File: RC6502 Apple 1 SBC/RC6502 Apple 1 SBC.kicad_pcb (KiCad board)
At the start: 2 copper layers, 99.1 x 99.7 mm, 43 parts, among them J1 VP GND, J2 Arduino Nano, J3 Backplane, J4 Hole, J5 Hole, J6 Hole, J7 Hole, J8 Power, SW1 RESET, U1 WD65C02, U2 HM62256BLP-7, U3 74HCT138, U4 28C256, U5 74HCT00, U6 NE555, U7 74HCT04, U8 WD65C21, U9 MCP23S17, X1 1MHz

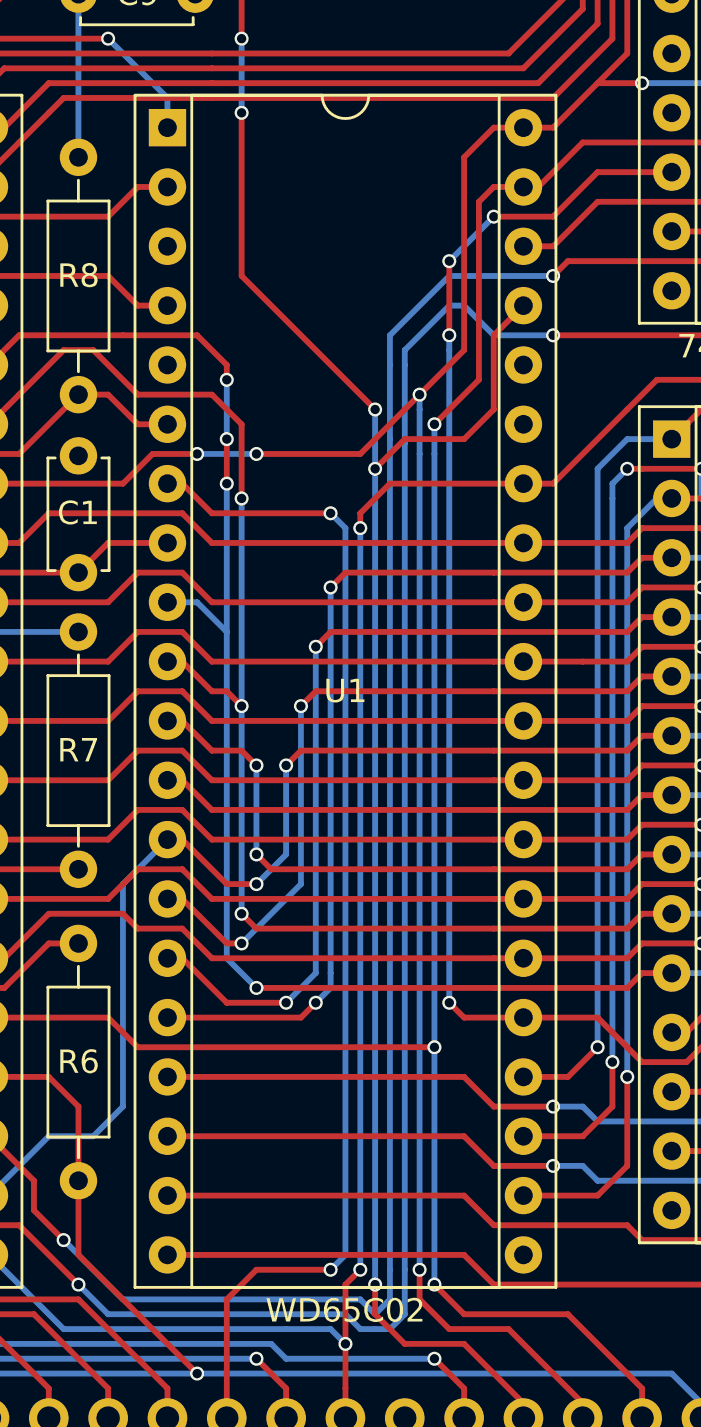
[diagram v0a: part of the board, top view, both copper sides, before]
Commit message: Added VP GND details to silkscreen.
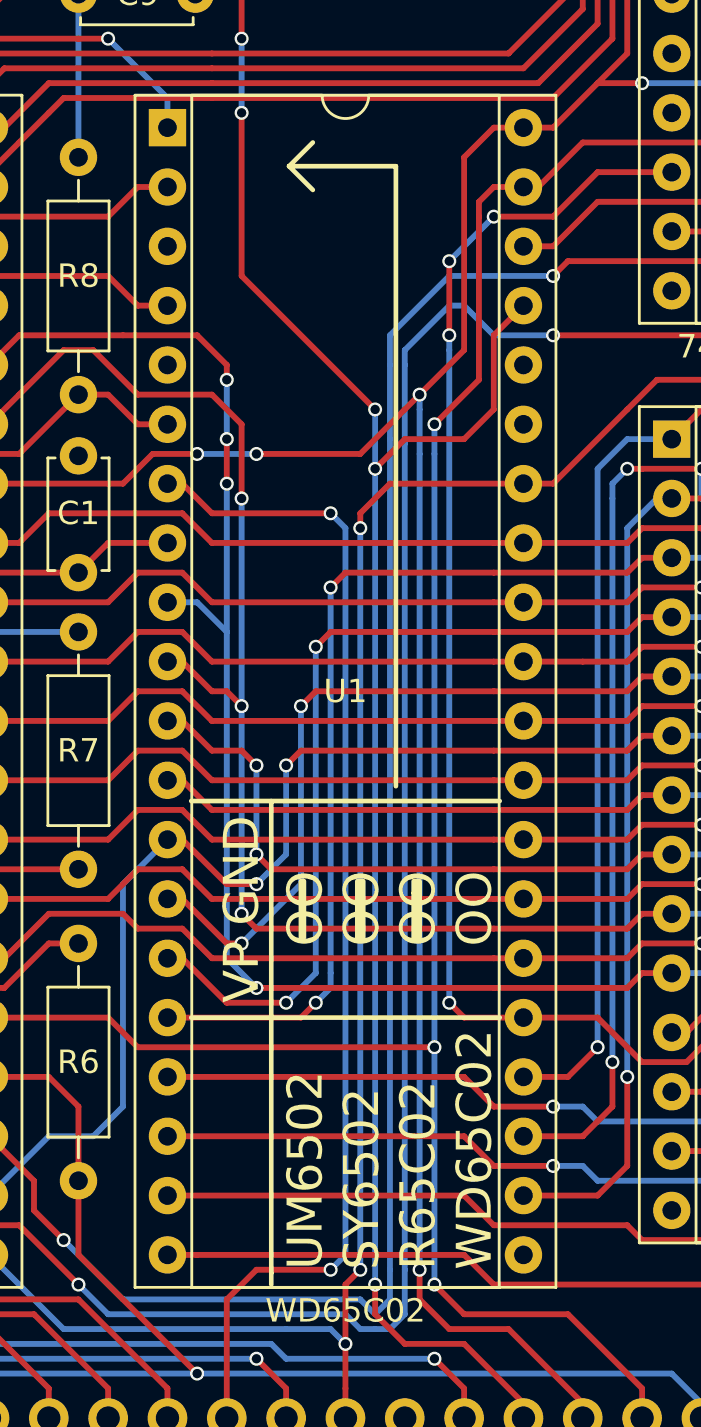
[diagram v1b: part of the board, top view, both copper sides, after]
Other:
- board text added: "OO OO OO OO"
- board text added: "UM6502 SY6502 R65C02 WD65C02"
- board text added: "VP GND"
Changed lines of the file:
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@@
     (links 229)
     (no_connects 0)
-    (area 114.23 35.22 220.820001 148.420001)
+    (area 116.129999 39.294999 215.340001 139.140001)
     (thickness 1.6)
-    (drawings 126)
+    (drawings 146)
     (tracks 1995)
     (zones 0)
@@
   (page A4)
   (layers
-    (0 F.Cu signal)
-    (31 B.Cu signal)
+    (0 F.Cu signal hide)
+    (31 B.Cu signal hide)
     (32 B.Adhes user)
     (33 F.Adhes user)
     (34 B.Paste user)
     (35 F.Paste user)
-    (36 B.SilkS user)
+    (36 B.SilkS user hide)
     (37 F.SilkS user)
     (38 B.Mask user)
@@
     )
   )
+  (gr_line (start 153.162 84.201) (end 154.178 85.217) (angle 90) (layer F.SilkS) (width 0.2))
+  (gr_line (start 153.162 84.201) (end 154.178 83.185) (angle 90) (layer F.SilkS) (width 0.2))
+  (gr_line (start 157.734 84.201) (end 153.162 84.201) (angle 90) (layer F.SilkS) (width 0.2))
+  (gr_line (start 157.734 110.744) (end 157.734 84.201) (angle 90) (layer F.SilkS) (width 0.2))
+  (gr_line (start 152.4 131.572) (end 152.4 132.08) (angle 90) (layer F.SilkS) (width 0.2))
+  (gr_line (start 156.337 117.221) (end 156.337 114.808) (angle 90) (layer F.SilkS) (width 0.2))
+  (gr_line (start 158.75 117.221) (end 158.75 114.808) (angle 90) (layer F.SilkS) (width 0.2))
+  (gr_line (start 158.496 115.316) (end 158.623 115.316) (angle 90) (layer F.SilkS) (width 0.2))
+  (gr_line (start 158.496 117.221) (end 158.496 114.808) (angle 90) (layer F.SilkS) (width 0.2))
+  (gr_line (start 158.623 117.221) (end 158.623 114.808) (angle 90) (layer F.SilkS) (width 0.2))
+  (gr_line (start 156.083 114.808) (end 156.083 117.221) (angle 90) (layer F.SilkS) (width 0.2))
+  (gr_line (start 156.21 117.221) (end 156.21 114.808) (angle 90) (layer F.SilkS) (width 0.2))
+  (gr_line (start 153.67 114.808) (end 153.67 117.221) (angle 90) (layer F.SilkS) (width 0.2))
+  (gr_line (start 153.797 114.808) (end 153.797 117.221) (angle 90) (layer F.SilkS) (width 0.2))
+  (gr_line (start 148.971 111.379) (end 162.179 111.379) (angle 90) (layer F.SilkS) (width 0.2))
+  (gr_line (start 148.971 120.65) (end 162.179 120.65) (angle 90) (layer F.SilkS) (width 0.2))
+  (gr_line (start 152.4 111.379) (end 152.4 131.572) (angle 90) (layer F.SilkS) (width 0.2))
+  (gr_text "VP GND" (at 151.13 120.015 90) (layer F.SilkS)
+    (effects (font (size 1.5 1.5) (thickness 0.2)) (justify left))
+  )
+  (gr_text "OO\nOO\nOO\nOO" (at 157.48 117.602 90) (layer F.SilkS)
+    (effects (font (size 1.5 1.5) (thickness 0.2)) (justify left))
+  )
+  (gr_text "UM6502\nSY6502\nR65C02\nWD65C02" (at 157.48 131.445 90) (layer F.SilkS)
+    (effects (font (size 1.5 1.5) (thickness 0.2)) (justify left))
+  )
   (gr_text "Backplane Connector" (at 156.21 134.62) (layer B.SilkS)

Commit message: Exported files with updated silkscreen
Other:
- board text added: "Jumper me when NOT using backplane"
- board text removed: "Jumper me when not using backplane"
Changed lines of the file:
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@@
     (area 116.129999 39.294999 215.340001 139.140001)
     (thickness 1.6)
-    (drawings 146)
+    (drawings 148)
     (tracks 1995)
     (zones 0)
@@
     (34 B.Paste user)
     (35 F.Paste user)
-    (36 B.SilkS user hide)
+    (36 B.SilkS user)
     (37 F.SilkS user)
     (38 B.Mask user)
@@
     )
   )
+  (gr_line (start 157.48 41.91) (end 158.75 41.91) (angle 90) (layer B.SilkS) (width 0.2))
+  (gr_line (start 157.48 46.99) (end 157.48 41.91) (angle 90) (layer B.SilkS) (width 0.2))
+  (gr_line (start 158.75 46.99) (end 157.48 46.99) (angle 90) (layer B.SilkS) (width 0.2))
+  (gr_text "Jumper me when\nNOT using backplane" (at 182.245 44.45) (layer B.SilkS)
+    (effects (font (size 1.5 1.5) (thickness 0.3)) (justify left mirror))
+  )
   (gr_line (start 153.162 84.201) (end 154.178 85.217) (angle 90) (layer F.SilkS) (width 0.2))
   (gr_line (start 153.162 84.201) (end 154.178 83.185) (angle 90) (layer F.SilkS) (width 0.2))
@@
   (gr_line (start 215.265 126.365) (end 212.725 126.365) (angle 90) (layer B.SilkS) (width 0.2))
   (gr_line (start 182.88 42.545) (end 182.88 46.355) (angle 90) (layer B.SilkS) (width 0.2))
-  (gr_text "Jumper me when\nnot using backplane" (at 182.245 44.45) (layer B.SilkS)
-    (effects (font (size 1.5 1.5) (thickness 0.3)) (justify left mirror))
-  )
   (gr_line (start 158.75 46.99) (end 186.055 46.99) (angle 90) (layer B.SilkS) (width 0.2))
-  (gr_line (start 158.75 41.91) (end 158.75 46.99) (angle 90) (layer B.SilkS) (width 0.2))
   (gr_line (start 186.055 41.91) (end 158.75 41.91) (angle 90) (layer B.SilkS) (width 0.2))
   (gr_line (start 186.055 46.99) (end 186.055 41.91) (angle 90) (layer B.SilkS) (width 0.2))

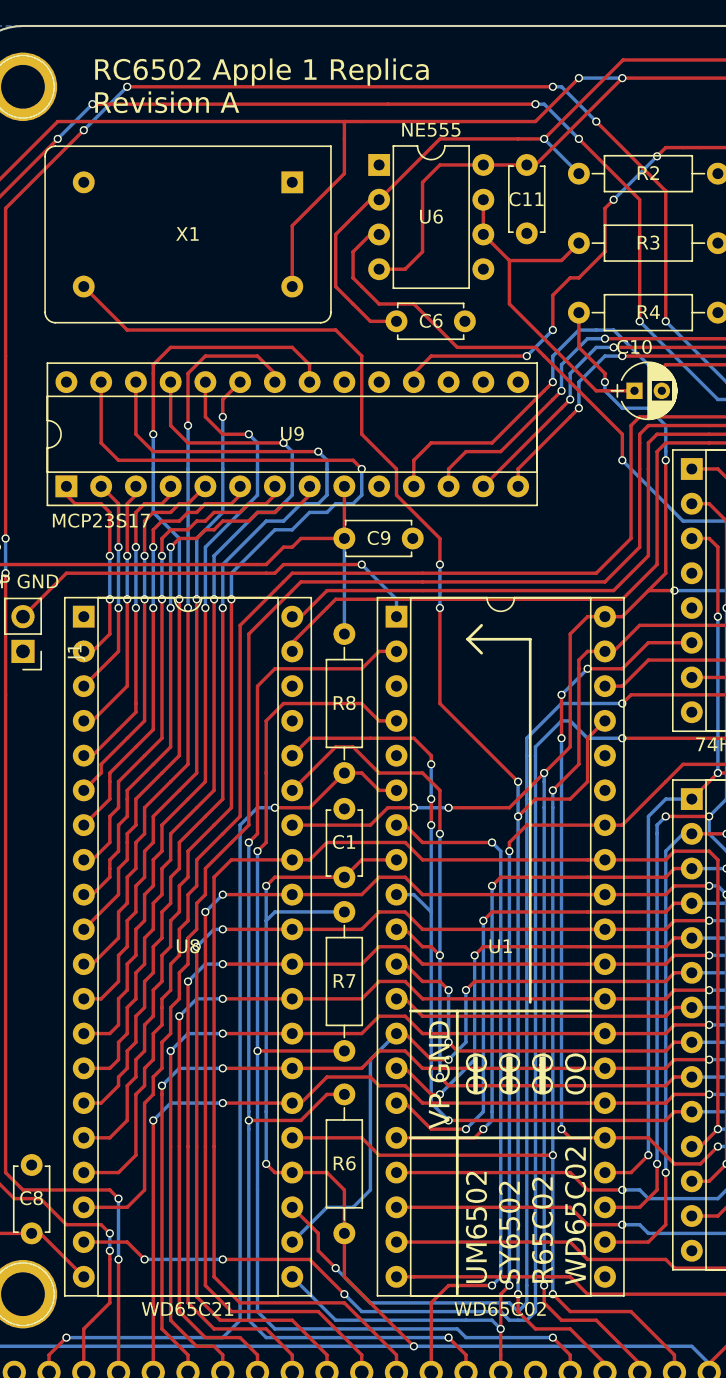
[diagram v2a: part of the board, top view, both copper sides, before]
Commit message: SBC Revision B
Revision A still don't work with W65c02 processors, added BE signal pull-up (untested wether this improves 65c02 compatibility).
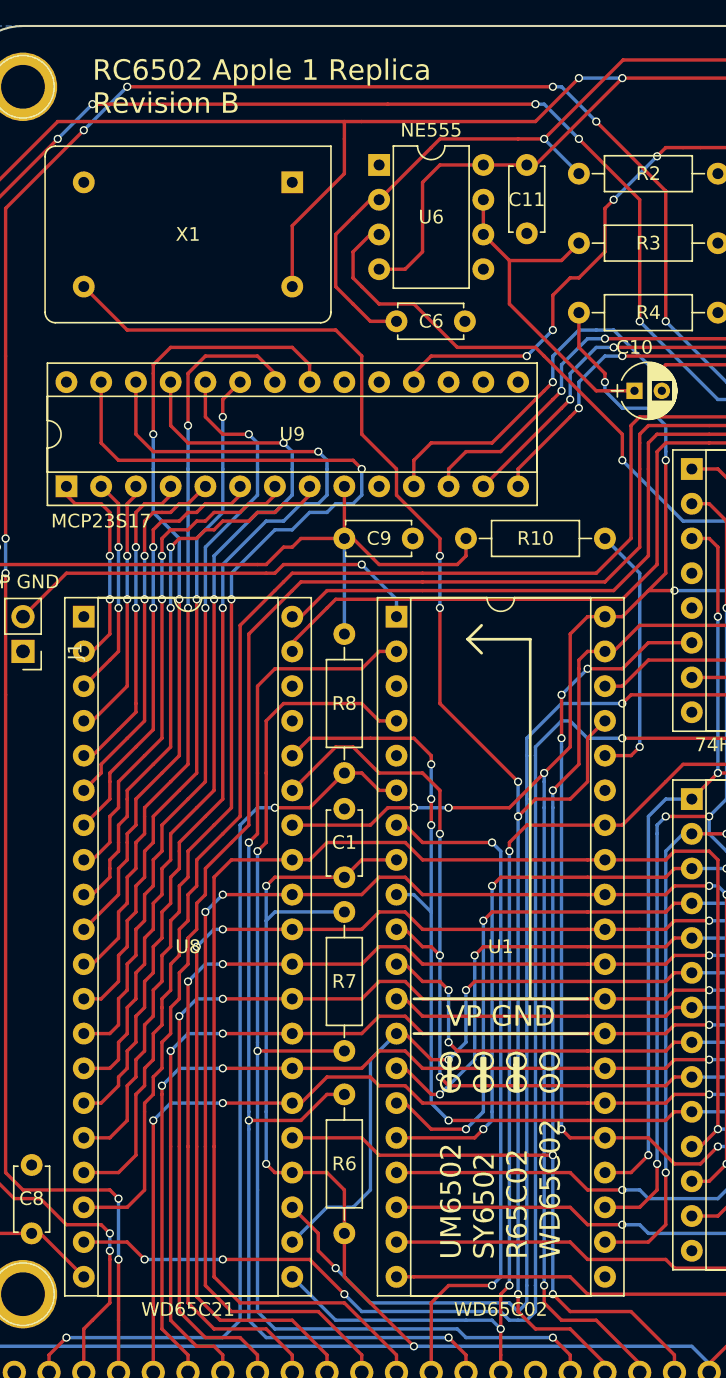
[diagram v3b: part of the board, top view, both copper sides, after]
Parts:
- added R10: 3.3k, Resistors_THT:R_Axial_DIN0207_L6.3mm_D2.5mm_P10.16mm_Horizontal, F.Cu at (163.2, 76.8)
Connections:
- U1 pad 36: (no net) -> Net-(R10-Pad1)
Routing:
- net Net-(R10-Pad1): track 0.00 -> 19.1 mm, vias 0 -> 1
- net VCC: track 645.7 -> 656.9 mm
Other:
- board text added: "Arduino I/O Expander"
- board text added: "Compile, upload and enjoy communication on your own terms!"
- board text added: "RC6502 Apple 1 Replica Revision B"
- board text added: "Signal inverter"
- board text removed: "Compile, upload and enjoy with your own changes!"
- board text removed: "HEX Inverter"
- board text removed: "IO Expander"
- board text removed: "RC6502 Apple 1 Replica Revision A"

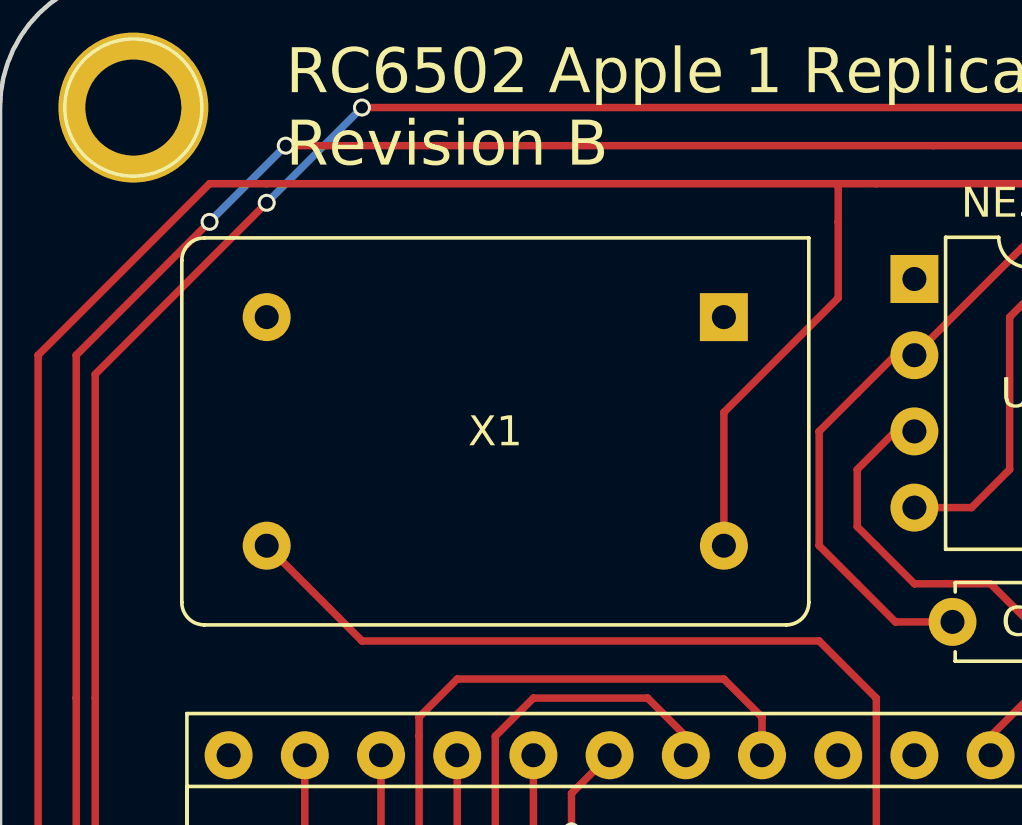
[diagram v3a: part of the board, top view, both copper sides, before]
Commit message: Moved oscillator right way up.
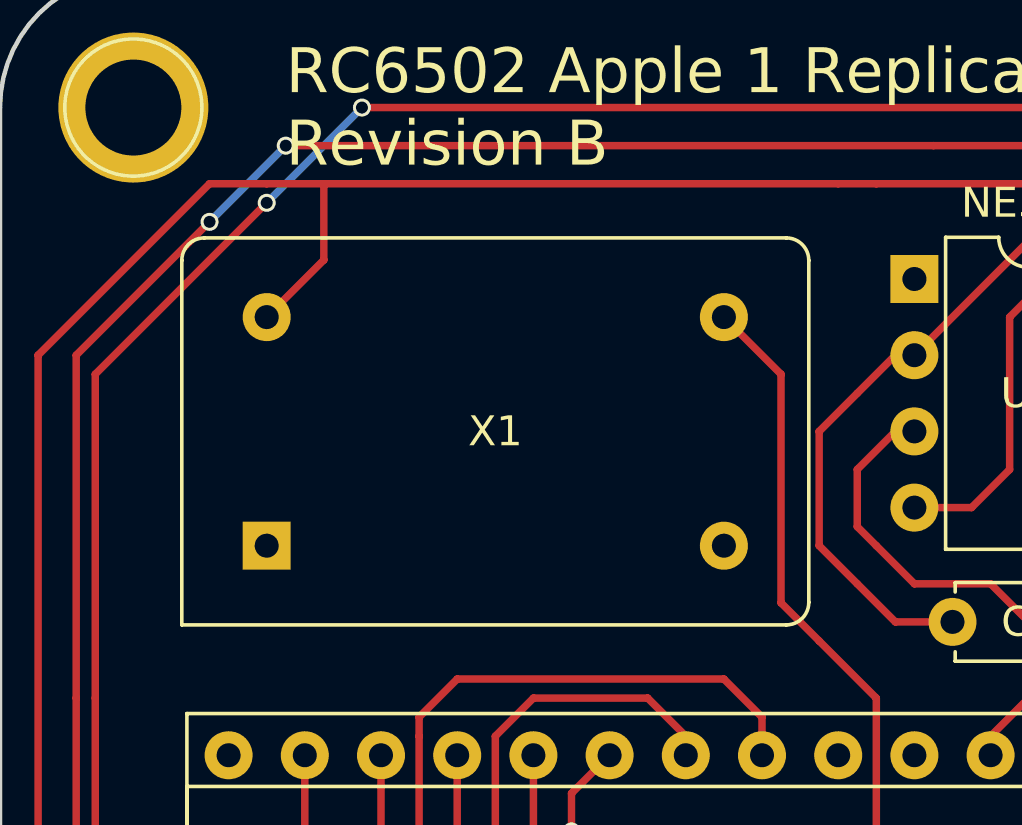
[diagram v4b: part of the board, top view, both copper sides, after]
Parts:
- moved X1 17.0 mm to (125.1, 58.4), turned to 0 degrees
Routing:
- net VCC: track 656.9 -> 648.5 mm
- net CLOCK: track 116.7 -> 109.1 mm

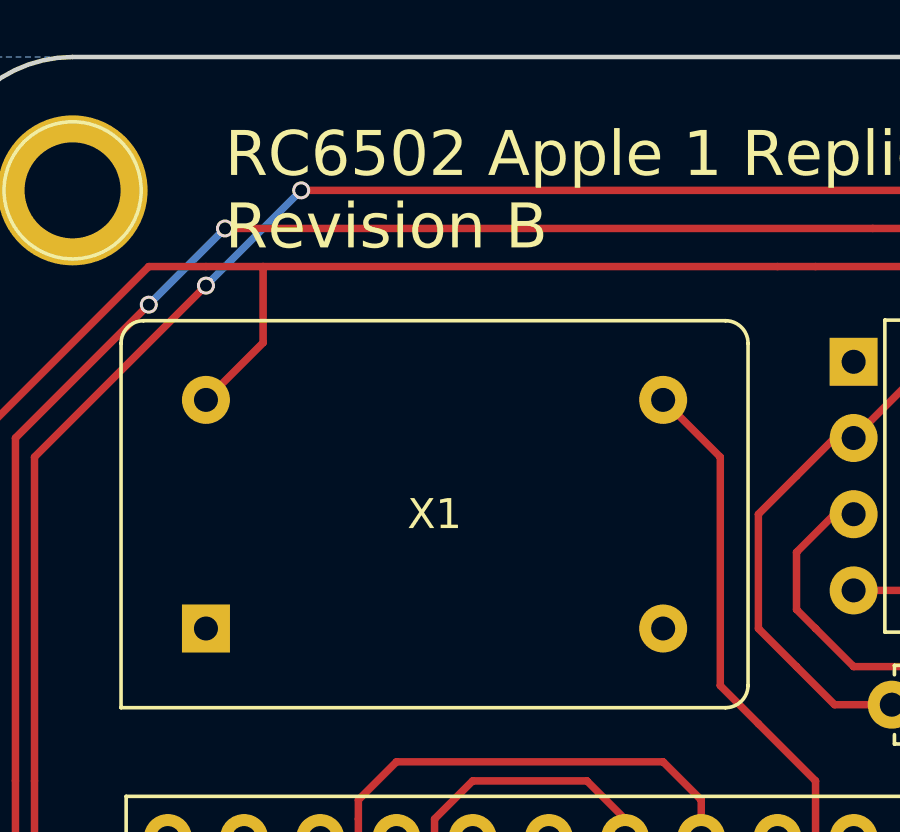
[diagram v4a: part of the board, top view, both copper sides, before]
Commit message: SBC uses new oscillator footprint
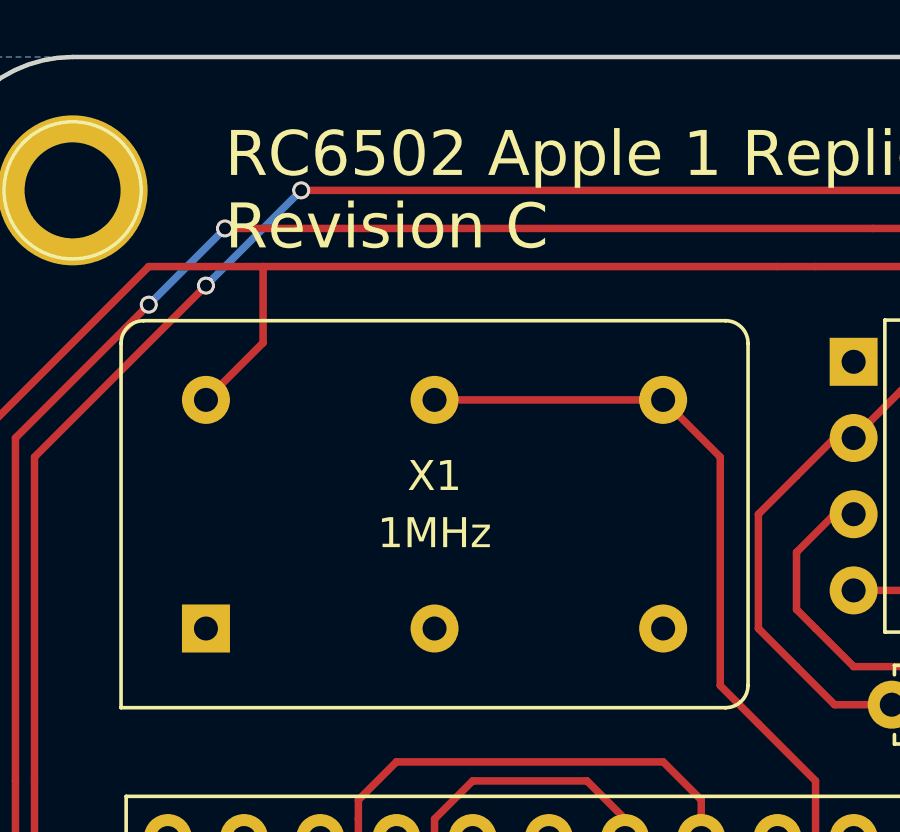
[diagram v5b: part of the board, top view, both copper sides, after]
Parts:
- X1: footprint Oscillators:Oscillator_DIP-14 -> Oscillator:Oscillator_DIP-14
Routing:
- net CLOCK: track 109.1 -> 116.7 mm
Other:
- board text added: "Jumper me when NOT using powered backplane"
- board text added: "RC6502 Apple 1 Replica Revision C"
- board text removed: "Jumper me when NOT using backplane"
- board text removed: "RC6502 Apple 1 Replica Revision B"
